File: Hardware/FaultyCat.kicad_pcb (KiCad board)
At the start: 2 copper layers, 51.2 x 124.2 mm, 118 parts, among them J1 Antenna, J2 BG306-02-A-2-0400-L-G, J3 Conn_01x10, J4 Header 2, J5 Header 4, J6 Input Power:2x AA Battery, P1 USB_C_Plug_USB2.0, Q1 AO3422, Q2 AO3422, Q3 LDA111STR, Q4 RGT16BM65DTL, Q5 DMG3415U-7, Q7 IRLML2502, Q8 IRF7807PBF, SW1 TL3305AF260QG, SW2 ON, SW3 TL3305AF260QG, SW4 RESET, SW5 BOOT, SW6 TL3305AF260QG, SW7 SW_SP3T, T1 ATB322524, T2 ATB322524, U1 AP2112K-3.3, U2 W25Q16JV, U3 RP2040, U4 TXB0108PW, U5 TLV75718PDBV, X1 BU-SMA, X2 BU-SMA, Y1 12Mhz

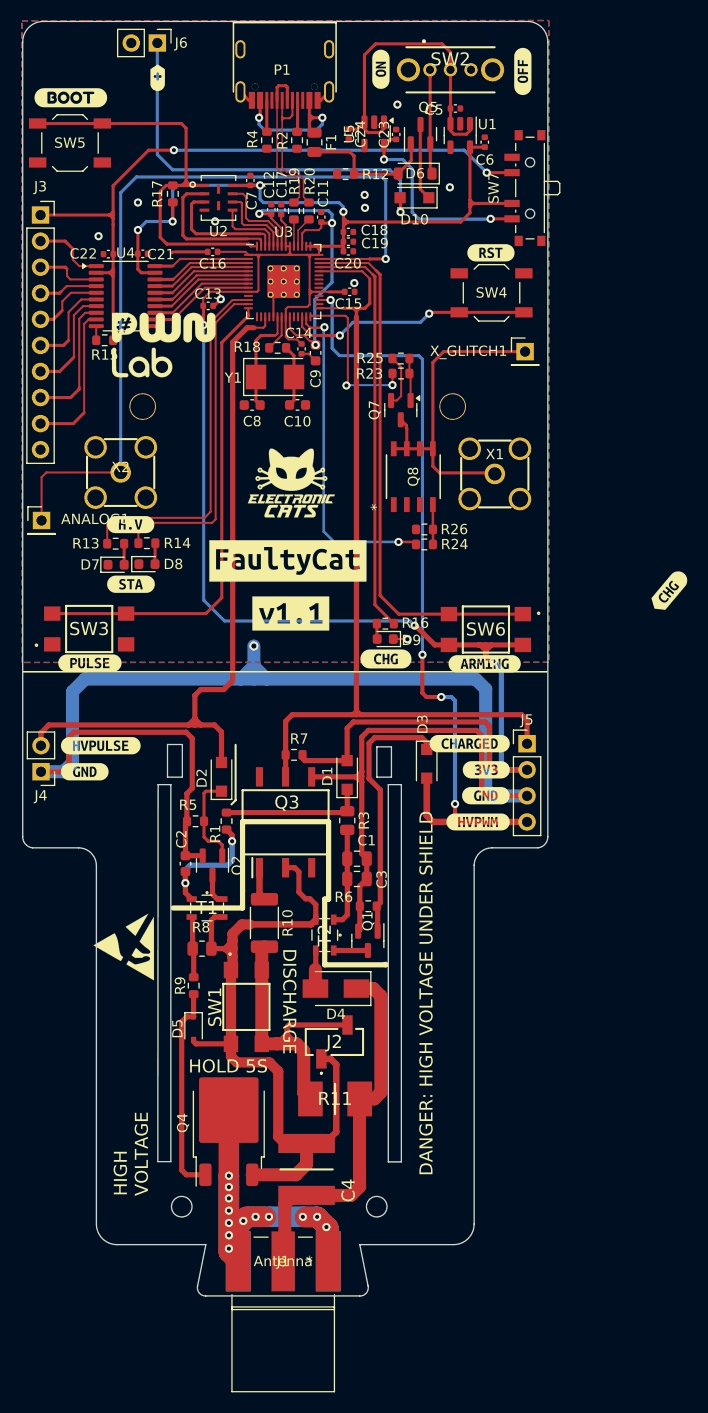
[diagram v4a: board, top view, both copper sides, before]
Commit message: feat(hw): add trigger pin and level shifter
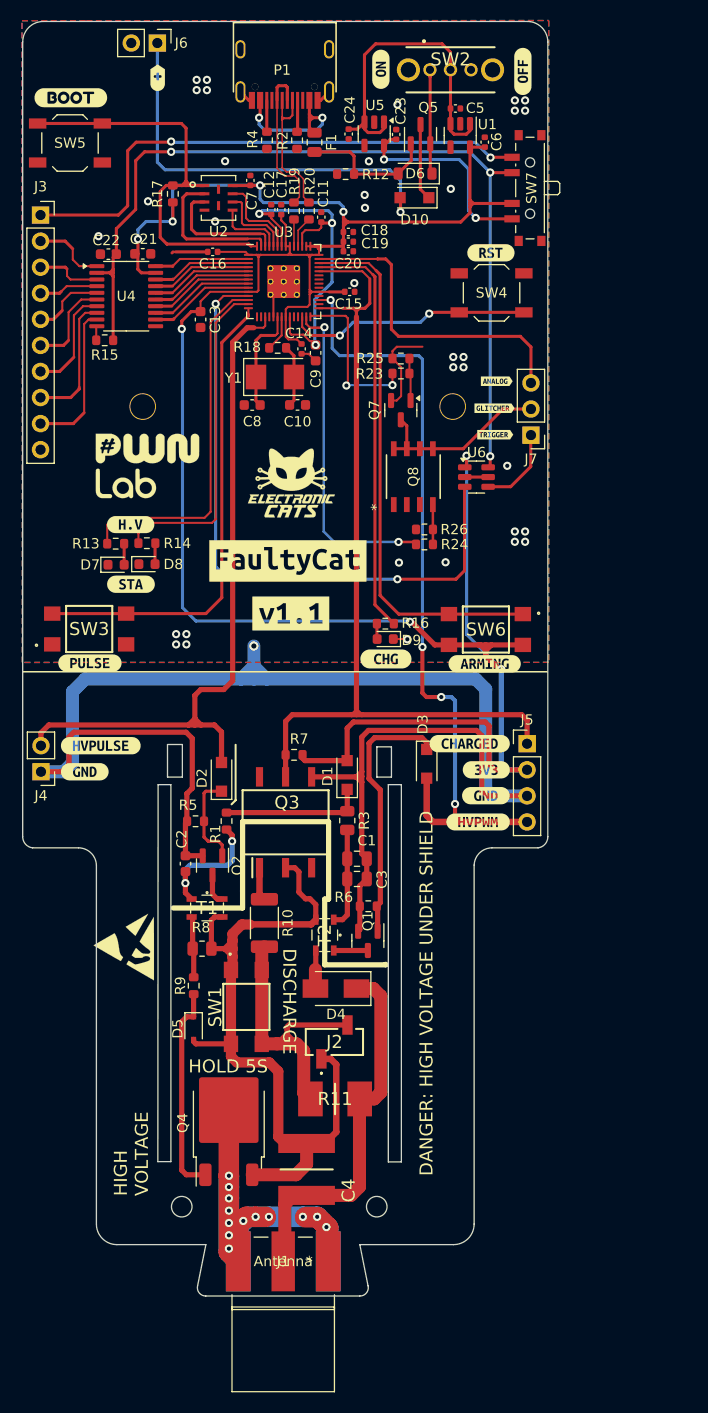
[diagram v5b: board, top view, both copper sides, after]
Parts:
- removed ANALOG1: ANALOG, Connector_PinHeader_2.54mm:PinHeader_1x01_P2.54mm_Vertical
- removed X1, X2: BU-SMA, BuggyCat:SMA-KE901
- removed X_GLITCH1: PINHDR_1X1, Connector_PinHeader_2.54mm:PinHeader_1x01_P2.54mm_Vertical
- removed kibuzzard-673E15C2: G***, kibuzzard-673E15C2
- added J7: Conn_01x03_Pin, Connector_PinHeader_2.54mm:PinHeader_1x03_P2.54mm_Vertical, F.Cu at (134.6, 65.6)
- added U6: SN74LVC1T45DBV, Package_TO_SOT_SMD:SOT-23-6, F.Cu at (129.3, 69.7)
- added kibuzzard-67A2921F: G***, kibuzzard-67A2921F, F.Cu at (131.2, 60.4)
- added kibuzzard-67A29228: G***, kibuzzard-67A29228, F.Cu at (131.0, 63.0)
- added kibuzzard-67A29236: G***, kibuzzard-67A29236, F.Cu at (131.1, 65.6)
- C13, C21, C22: footprint Capacitor_SMD:C_0402_1005Metric -> Capacitor_SMD:C_0603_1608Metric
- U4: value TXB0108PW -> TXS0108EPW
- moved G*** 11.9 mm to (97.2, 68.6)
- moved C13 1.52 mm to (102.4, 54.4), turned to -90 degrees
- moved U4 0.06 mm to (95.1, 52.1)
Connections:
- C22 pad 1: /VREF -> /VREFOUT
- R15 pad 1: /VREF -> /VREFOUT
- SW7 pad 3: /VREF -> /VREFOUT
- SW7 pad 4: unconnected-(SW7-Pad4) -> /VREF
- U3 pad 11: unconnected-(U3-GPIO8-Pad11) -> /TRIGGER
- U4 pad 2: /VREF -> /VREFOUT
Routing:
- net /VREFOUT: track 0.00 -> 88.1 mm, vias 0 -> 3
- net /TRIGGER: track 0.00 -> 62.4 mm, vias 0 -> 2
- net /ANALOG: track 80.2 -> 31.4 mm, vias 1 -> 0
- net +3V3: track 222.4 -> 249.9 mm, vias 7 -> 8
- net Net-(J7-Pin_2): track 32.8 -> 18.0 mm
- net /VREF: track 66.9 -> 52.7 mm
- net /TRIGGER_IN: track 0.00 -> 8.05 mm
- net GND: track 169.8 -> 174.5 mm, vias 11 -> 35

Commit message: feat(hw): change position of pins
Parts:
- removed kibuzzard-67A2921F: G***, kibuzzard-67A2921F
- removed kibuzzard-67A29228: G***, kibuzzard-67A29228
- removed kibuzzard-67A29236: G***, kibuzzard-67A29236
- added J10: TRIGGER_VREF, Connector_PinSocket_2.54mm:PinSocket_1x02_P2.54mm_Vertical, F.Cu at (86.5, 77.6)
- added J8: ANALOG_PINS, Connector_PinSocket_2.54mm:PinSocket_1x02_P2.54mm_Vertical, F.Cu at (86.5, 56.6)
- added J9: TRIGGER_IN, Connector_PinSocket_2.54mm:PinSocket_1x02_P2.54mm_Vertical, F.Cu at (86.5, 71.4)
- added R21: R, Resistor_SMD:R_0603_1608Metric, F.Cu at (92.1, 70.8)
- added R22: R, Resistor_SMD:R_0603_1608Metric, F.Cu at (92.1, 75.8)
- J7: value Conn_01x03_Pin -> GLITCHER_EN; footprint Connector_PinHeader_2.54mm:PinHeader_1x03_P2.54mm_Vertical -> Connector_PinSocket_2.54mm:PinSocket_1x02_P2.54mm_Vertical
- moved J7 48.1 mm to (86.5, 65.2)
- moved U6 37.3 mm to (92.1, 73.3), turned to 180 degrees
- moved J3 14.0 mm to (86.5, 30.2)
- moved G*** 14.0 mm to (111.2, 69.5)
- moved kibuzzard-642DF5C4 11.3 mm to (99.5, 38.4)
- moved SW5 10.4 mm to (99.6, 34.2), turned to 0 degrees
- moved kibuzzard-642DF578 10.2 mm to (130.6, 58.0)
- moved G*** 6.20 mm to (111.0, 76.5)
- moved kibuzzard-64767B55 5.92 mm to (103.8, 28.8), turned to 180 degrees
- moved Q8 5.62 mm to (128.5, 71.4)
- moved R23 5.47 mm to (123.3, 64.9)
- moved R25 5.42 mm to (123.3, 63.4)
- moved Q7 4.71 mm to (123.2, 67.7)
- moved kibuzzard-6475468D 4.50 mm to (110.7, 82.4)
- moved R26 4.03 mm to (128.0, 76.0)
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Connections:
- J7 pad 1: /TRIGGER_IN -> /GLITCHER
- J7 pad 2: Net-(J7-Pin_2) -> /GLITCHER
- Q7 pad 3: Net-(J7-Pin_2) -> /GLITCHER
- Q8 pad 5: Net-(J7-Pin_2) -> /GLITCHER
- Q8 pad 6: Net-(J7-Pin_2) -> /GLITCHER
- Q8 pad 7: Net-(J7-Pin_2) -> /GLITCHER
- Q8 pad 8: Net-(J7-Pin_2) -> /GLITCHER
- U6 pad 5: GND -> Net-(U6-DIR)
- U6 pad 6: /VREFOUT -> /TRIGGER_VREF
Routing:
- net /GLITCHER: track 0.00 -> 49.5 mm, vias 0 -> 3
- net /TRIGGER: track 62.4 -> 32.8 mm
- net /VREFOUT: track 88.1 -> 59.9 mm, vias 3 -> 2
- net /ANALOG: track 31.4 -> 55.2 mm, vias 0 -> 3
- net Net-(J7-Pin_2): track 18.0 -> 0.00 mm
- net Net-(J3-Pin_2): track 7.11 -> 21.1 mm
- net +3V3: track 249.9 -> 236.6 mm
- net Net-(J3-Pin_3): track 6.33 -> 19.2 mm
- net Net-(J3-Pin_4): track 5.72 -> 17.0 mm
- net /QSPI_CS: track 40.3 -> 30.4 mm
- net Net-(J3-Pin_5): track 7.08 -> 15.3 mm
- net Net-(U6-DIR): track 0.00 -> 8.06 mm
- net Net-(J3-Pin_9): track 14.7 -> 6.96 mm
- net /TRIGGER_VREF: track 0.00 -> 7.38 mm
- net /HPGLITCH2: track 32.1 -> 37.3 mm
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
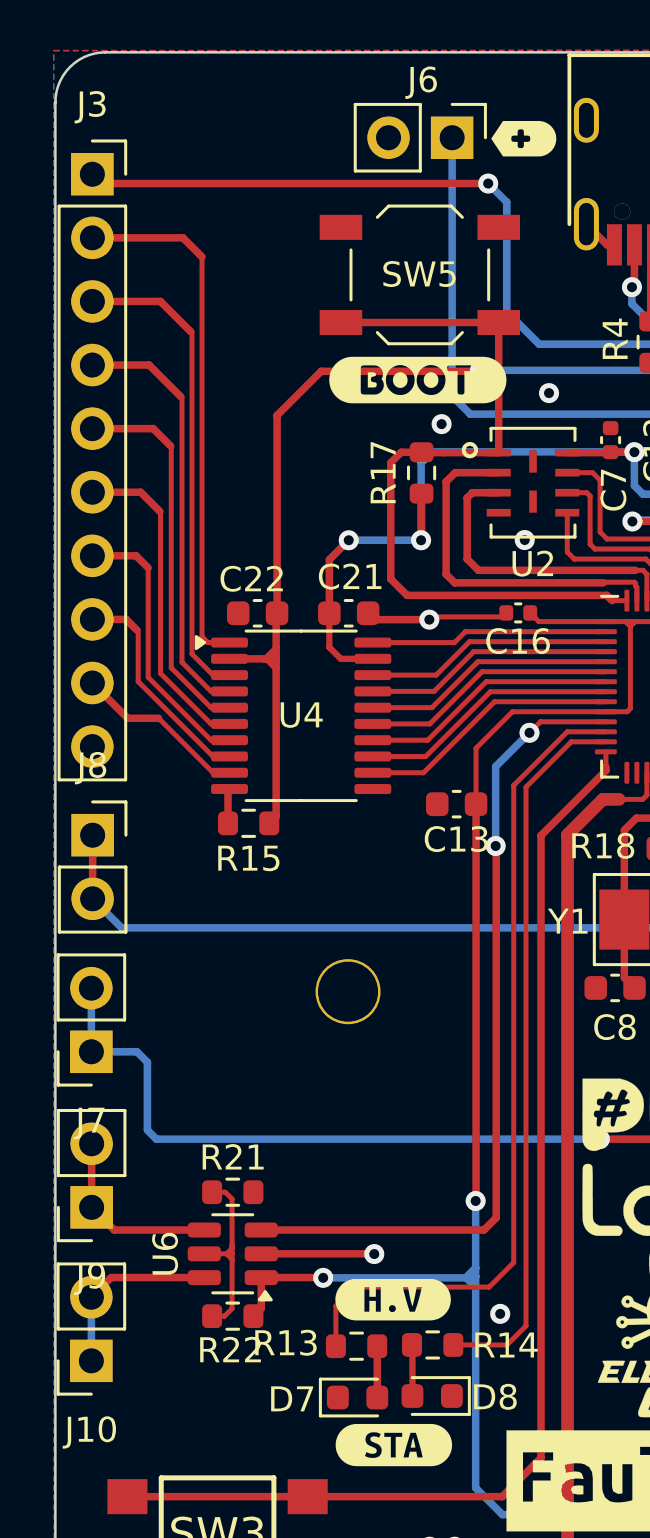
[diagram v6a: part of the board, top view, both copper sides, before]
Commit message: feat(hw): add labels
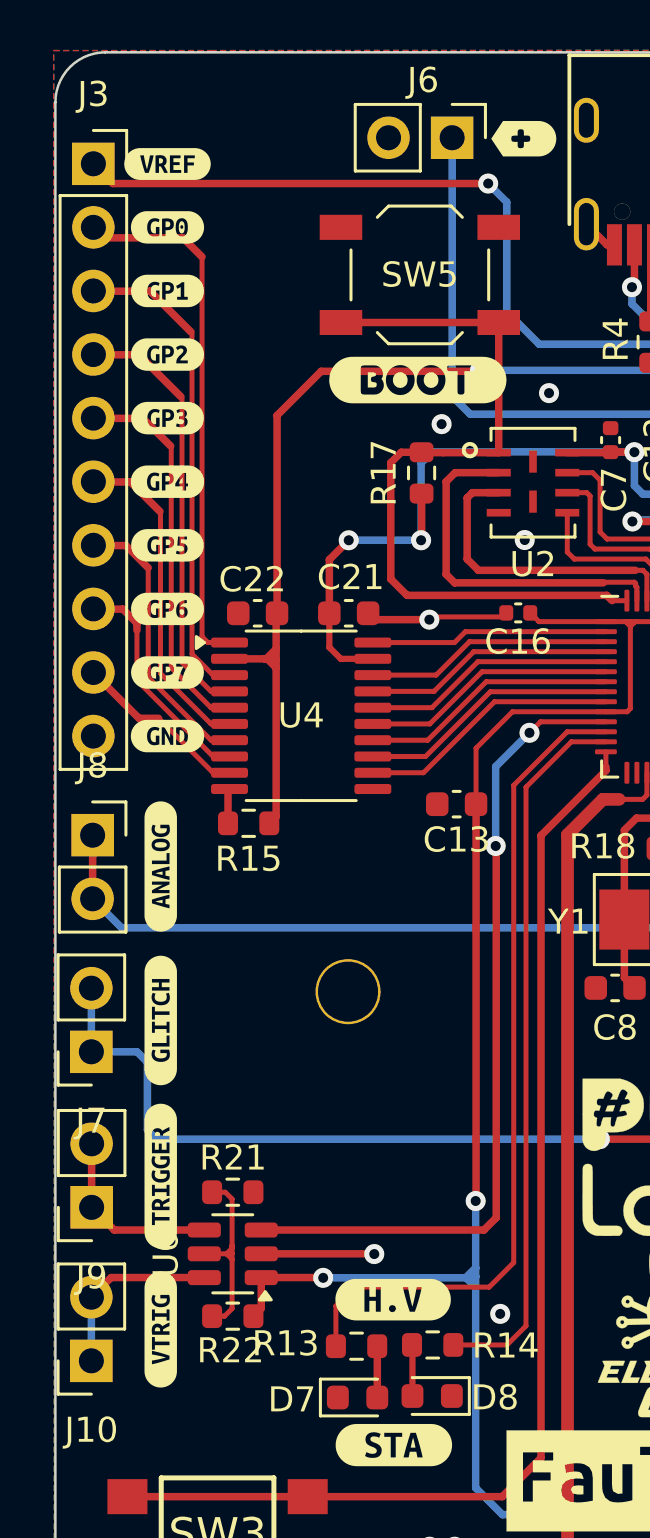
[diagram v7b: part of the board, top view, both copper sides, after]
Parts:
- added kibuzzard-67A4D63C: G***, kibuzzard-67A4D63C, F.Cu at (89.3, 57.8)
- added kibuzzard-67A4D642: G***, kibuzzard-67A4D642, F.Cu at (89.3, 64.0)
- added kibuzzard-67A4D648: G***, kibuzzard-67A4D648, F.Cu at (89.3, 70.2)
- added kibuzzard-67A4D65E: G***, kibuzzard-67A4D65E, F.Cu at (89.3, 76.3)
- added kibuzzard-67A4D805: G***, kibuzzard-67A4D805, F.Cu at (89.5, 29.8)
- added kibuzzard-67A4D80D: G***, kibuzzard-67A4D80D, F.Cu at (89.5, 32.3)
- added kibuzzard-67A4D86D: G***, kibuzzard-67A4D86D, F.Cu at (89.5, 34.8)
- added kibuzzard-67A4D873: G***, kibuzzard-67A4D873, F.Cu at (89.5, 37.4)
- added kibuzzard-67A4D879: G***, kibuzzard-67A4D879, F.Cu at (89.5, 39.9)
- added kibuzzard-67A4D880: G***, kibuzzard-67A4D880, F.Cu at (89.5, 42.5)
- added kibuzzard-67A4D886: G***, kibuzzard-67A4D886, F.Cu at (89.5, 45.0)
- added kibuzzard-67A4D88F: G***, kibuzzard-67A4D88F, F.Cu at (89.5, 47.5)
- added kibuzzard-67A4D896: G***, kibuzzard-67A4D896, F.Cu at (89.5, 50.1)
- added kibuzzard-67A4D93E: G***, kibuzzard-67A4D93E, F.Cu at (89.5, 52.6)
- moved J3 0.42 mm to (86.6, 29.8)

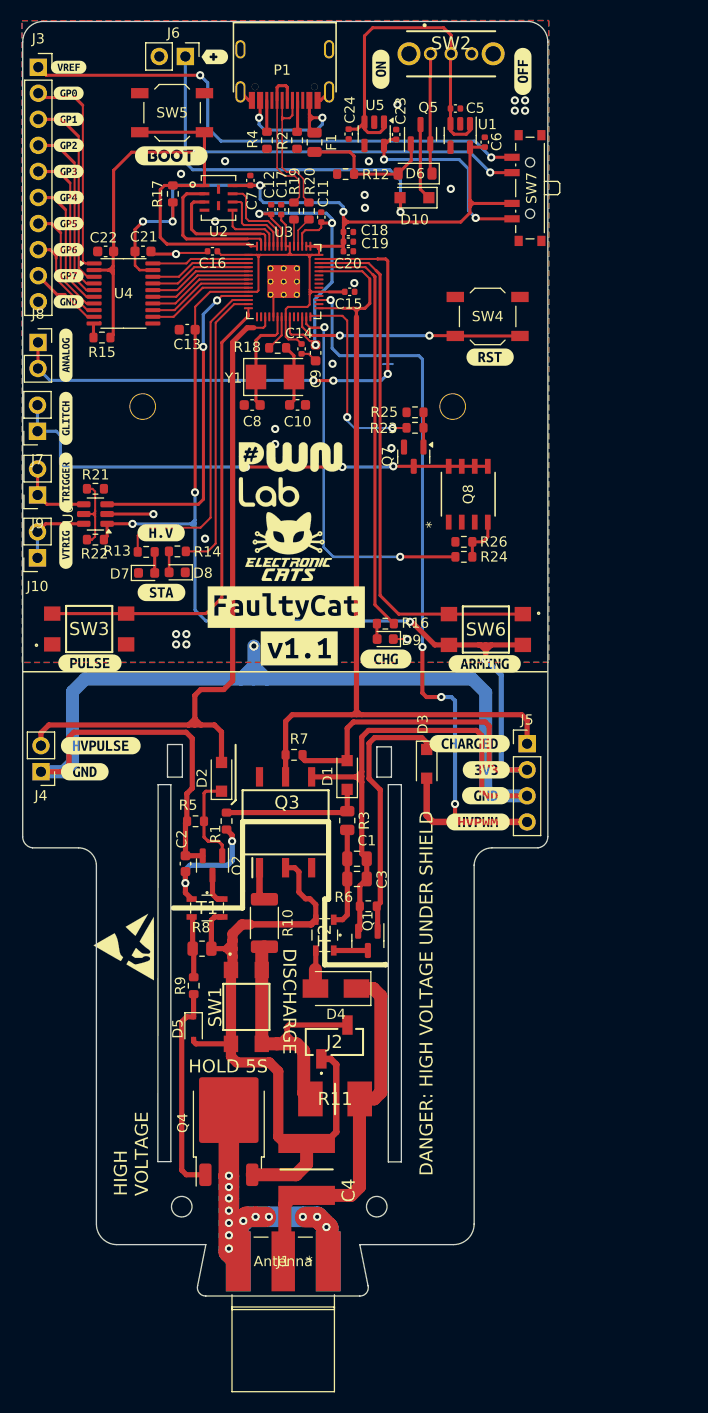
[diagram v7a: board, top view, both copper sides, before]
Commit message: feat(Hw):Update_Labels
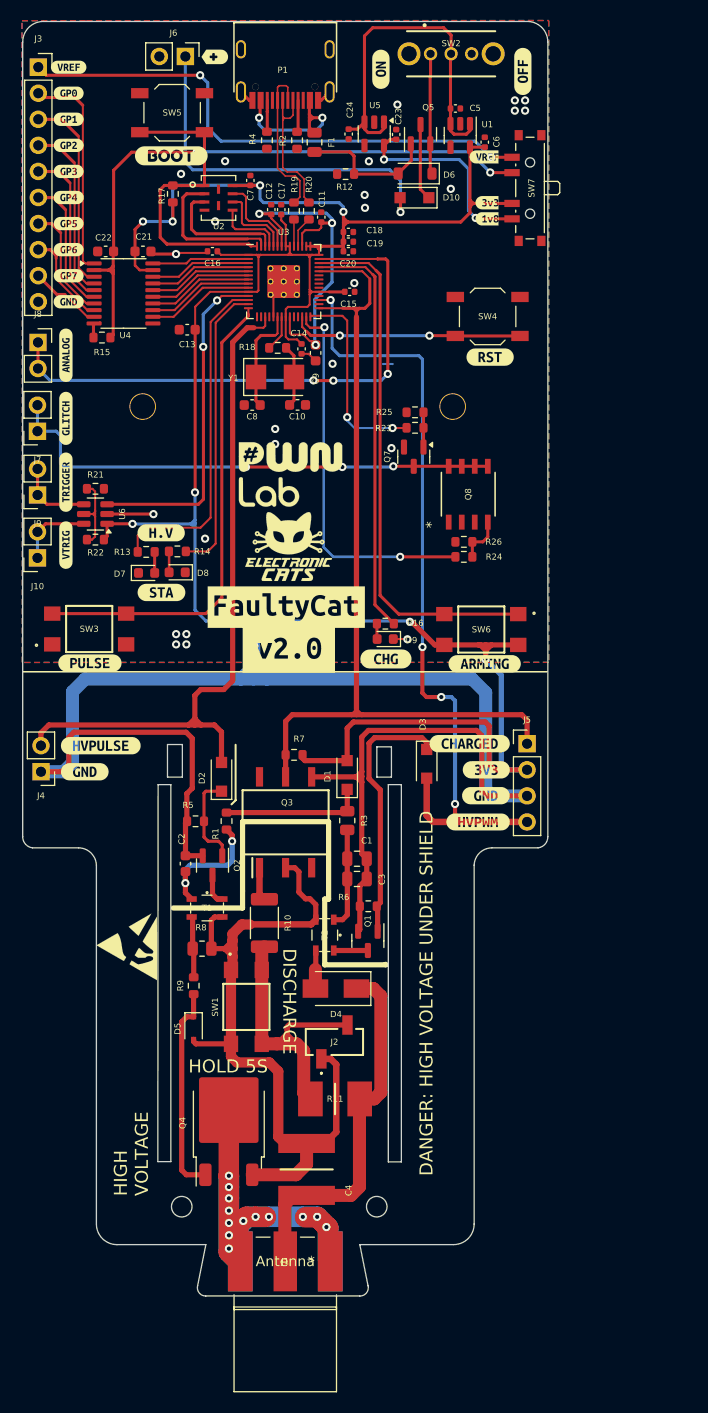
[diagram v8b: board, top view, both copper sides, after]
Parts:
- removed kibuzzard-647546C2: G***, kibuzzard-647546C2
- added kibuzzard-67AA305E: G***, kibuzzard-67AA305E, F.Cu at (111.0, 86.4)
- added kibuzzard-67AA359F: G***, kibuzzard-67AA359F, F.Cu at (130.3, 44.5)
- added kibuzzard-67AA35B7: G***, kibuzzard-67AA35B7, F.Cu at (130.3, 43.0)
- added kibuzzard-67AA35C3: G***, kibuzzard-67AA35C3, F.Cu at (130.0, 38.5)
- moved SW6 0.45 mm to (129.7, 84.5)
- moved REF** 0.30 mm to (95.2, 115.5)
- moved J1 0.20 mm to (110.6, 147.3)
